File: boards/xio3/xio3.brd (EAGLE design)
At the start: 170 x 170 mm, 67 parts, among them J1 POWER_JACKPTH

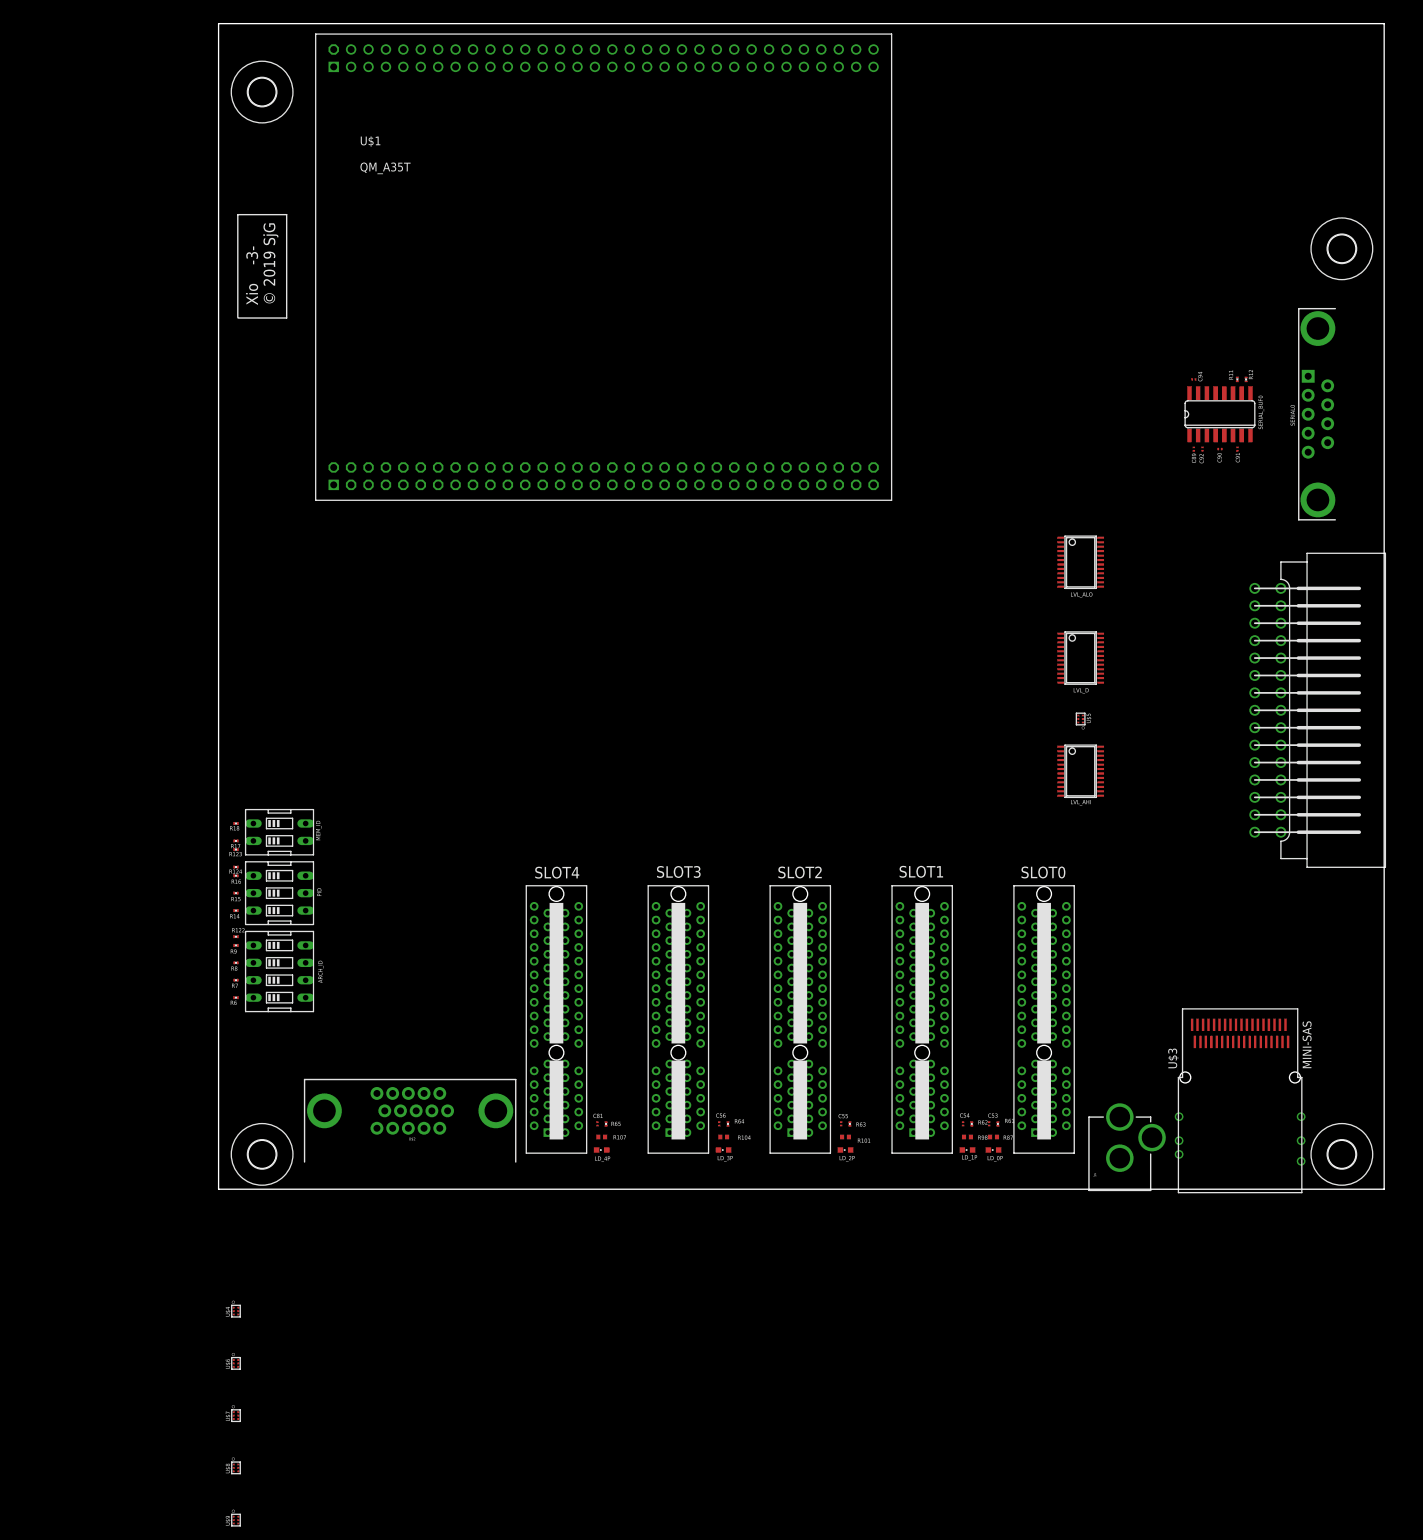
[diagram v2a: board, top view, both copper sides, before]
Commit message: Before deciding which signals to drop for S4,S5
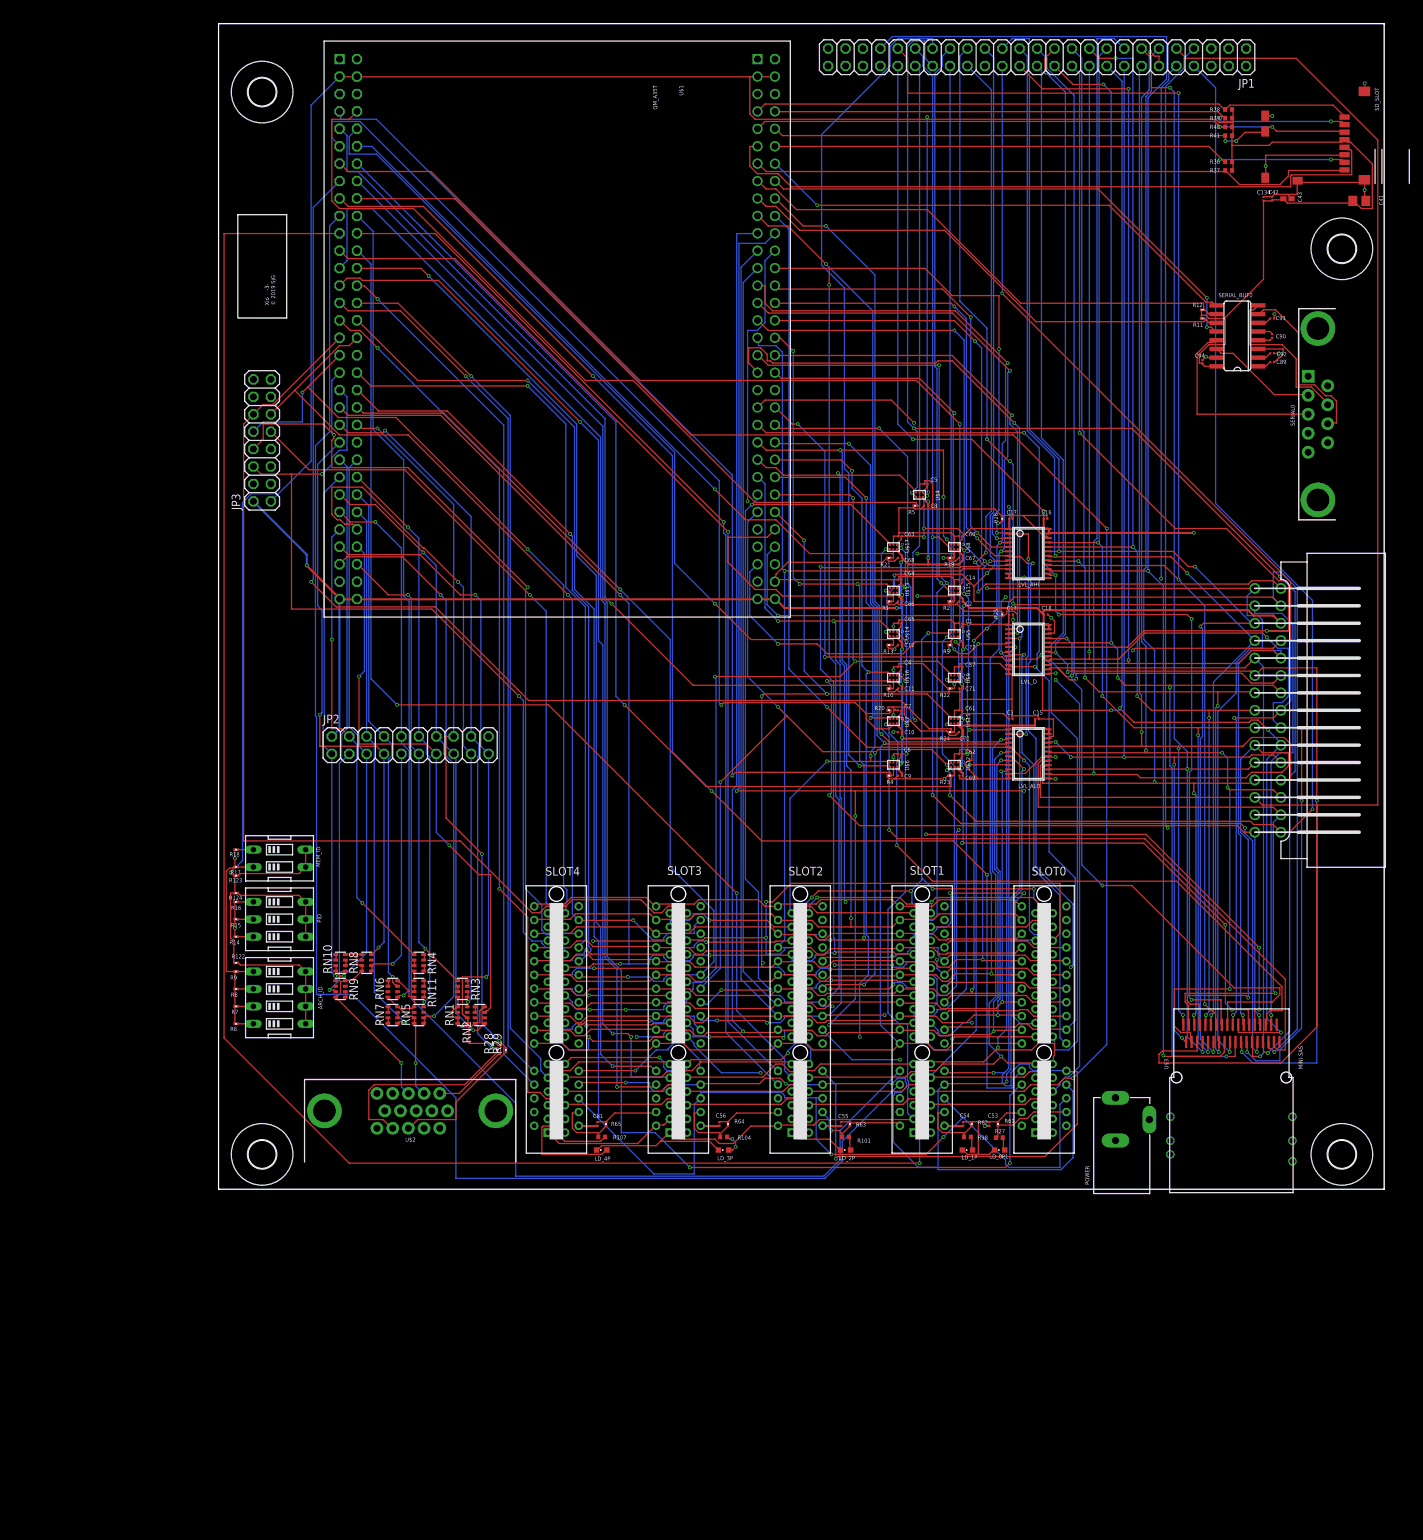
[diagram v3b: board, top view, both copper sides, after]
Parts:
- removed J1: POWER_JACKPTH, SparkFun:POWER_JACK_PTH
- removed LD_0P: SML-D12D1WT86, led:CHIPLED_0603
- removed R87: 59R, rcl:R0402
- added C1, C10, C11, C12, C13, C134, C14, C15, C16, C17, C18, C2, C3, C4, C5, C57, C6, C60, C61, C62, C63, C64, C65, C66, C67, C68, C69, C7, C70, C71, C72, C8, C9: 0.1uF, rcl:C0201
- added C41: 22uF, rcl:C0805
- added C42: 1uF, rcl:C0201
- added C43: 10uF, rcl:C0402K
- added JP1: (no value), pinhead:2X25
- added JP2: (no value), pinhead:2X10
- added JP3: (no value), pinhead:2X08
- added LD_0P1: SML-D12D1WT86, led:CHIPLED_0603
- added POWER: dc5vin, sjg-power:DCJ3P-14.2X11.0X9.0MM
- added R1, R10, R13, R19, R2, R20, R21, R22, R23, R24, R25, R26, R3, R4, R5: 10K, rcl:R0201
- added R27: 59R, rcl:R0402
- added R28, R29: 100R, rcl:R0201
- added R36, R37, R38, R39, R40, R41: 4K7, rcl:R0402
- added RN1, RN5, RN8: 1K, sjg-resistor:ACAS0612
- added RN10, RN11, RN2, RN3, RN4, RN6, RN7, RN9: 2K, sjg-resistor:ACAS0612
- added SD_SLOT: 5025700893, j_microsd_molex_5025700893:5025700893
- added U$11, U$12, U$13, U$14, U$15, U$16, U$17: 74LVC1T45GWSOT866, sjg-logic:SOT886
- moved U$8 170.3 mm to (107.3, 93.7), turned to 270 degrees
- moved U$9 161.5 mm to (107.3, 74.6), turned to 270 degrees
- moved U$4 155.3 mm to (102.2, 101.3), turned to 270 degrees
- moved U$7 139.5 mm to (98.4, 68.3), turned to 270 degrees
- moved U$6 129.7 mm to (98.4, 61.9), turned to 270 degrees
- moved LVL_AHI 32.7 mm to (118.1, 92.7)
- moved LVL_ALO 29.0 mm to (118.1, 63.5)
- moved U$5 22.2 mm to (107.3, 81.0), turned to 270 degrees
- moved C91 19.7 mm to (153.7, 127.0), turned to 0 degrees
- moved C90 18.2 mm to (153.7, 124.5), turned to 270 degrees
- moved C92 17.3 mm to (153.7, 121.9), turned to 0 degrees
- moved C89 17.1 mm to (153.7, 120.7), turned to 180 degrees
- moved R12 12.0 mm to (143.5, 128.3), turned to 0 degrees
- moved SERIAL_BUF0 11.7 mm to (148.6, 124.5), turned to 90 degrees
- moved U$1 11.3 mm to (49.4, 125.5), turned to 270 degrees
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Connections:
- removed net !H_CCTL!: CARTRIDGE.P15
- removed net !H_EXTSEL!: U$3.PB13
- removed net !H_HALT!: U$3.PA14
- removed net !H_IRQ!: U$3.PB14
- removed net !H_MPD!: U$3.PA15
- removed net !H_RST!: U$3.PA17
- removed net !H_S4!: CARTRIDGE.P1
- removed net !H_S5!: CARTRIDGE.P12
- removed net HOST_!EXTSEL!: SLOT0.B26, SLOT1.B26, SLOT2.B26, SLOT3.B26, SLOT4.B26
- removed net HOST_!HALT!: SLOT0.B27, SLOT1.B27, SLOT2.B27, SLOT3.B27, SLOT4.B27
- removed net HOST_!IRQ!: SLOT0.B28, SLOT1.B28, SLOT2.B28, SLOT3.B28, SLOT4.B28
- removed net HOST_!MPD!: SLOT0.B29, SLOT1.B29, SLOT2.B29, SLOT3.B29, SLOT4.B29
- removed net HOST_!REF!: SLOT0.B30, SLOT1.B30, SLOT2.B30, SLOT3.B30, SLOT4.B30
- removed net HOST_!RST!: SLOT0.B31, SLOT1.B31, SLOT2.B31, SLOT3.B31, SLOT4.B31
- removed net HOST_A0: SLOT0.A8, SLOT1.A8, SLOT2.A8, SLOT3.A8, SLOT4.A7
- removed net HOST_A1: SLOT0.A9, SLOT1.A9, SLOT2.A9, SLOT3.A9, SLOT4.A8
- removed net HOST_A10: SLOT0.A18, SLOT1.A18, SLOT2.A18, SLOT3.A18, SLOT4.A17
- removed net HOST_A11: SLOT0.A19, SLOT1.A19, SLOT2.A19, SLOT3.A19, SLOT4.A18
- removed net HOST_A12: SLOT0.A20, SLOT1.A20, SLOT2.A20, SLOT3.A20, SLOT4.A19
- removed net HOST_A13: SLOT0.A21, SLOT1.A21, SLOT2.A21, SLOT3.A21, SLOT4.A20
- removed net HOST_A14: SLOT0.A22, SLOT1.A22, SLOT2.A22, SLOT3.A22, SLOT4.A21
- removed net HOST_A15: SLOT0.A23, SLOT1.A23, SLOT2.A23, SLOT3.A23, SLOT4.A22
- removed net HOST_A2: SLOT0.A10, SLOT1.A10, SLOT2.A10, SLOT3.A10, SLOT4.A9
- removed net HOST_A3: SLOT0.A11, SLOT1.A11, SLOT2.A11, SLOT3.A11, SLOT4.A10
- removed net HOST_A4: SLOT0.A12, SLOT1.A12, SLOT2.A12, SLOT3.A12, SLOT4.A11
- removed net HOST_A5: SLOT0.A13, SLOT1.A13, SLOT2.A13, SLOT3.A13, SLOT4.A12
- removed net HOST_A6: SLOT0.A14, SLOT1.A14, SLOT2.A14, SLOT3.A14, SLOT4.A13
- removed net HOST_A7: SLOT0.A15, SLOT1.A15, SLOT2.A15, SLOT3.A15, SLOT4.A14
- removed net HOST_A8: SLOT0.A16, SLOT1.A16, SLOT2.A16, SLOT3.A16, SLOT4.A15
- removed net HOST_A9: SLOT0.A17, SLOT1.A17, SLOT2.A17, SLOT3.A17, SLOT4.A16
- removed net HOST_CLK: SLOT0.A24, SLOT1.A24, SLOT2.A24, SLOT3.A24, SLOT4.A23
- removed net HOST_D0: SLOT0.A25, SLOT1.A25, SLOT2.A25, SLOT3.A25, SLOT4.A24
- removed net HOST_D1: SLOT0.A26, SLOT1.A26, SLOT2.A26, SLOT3.A26, SLOT4.A25
- removed net HOST_D2: SLOT0.A27, SLOT1.A27, SLOT2.A27, SLOT3.A27, SLOT4.A26
- removed net HOST_D3: SLOT0.A28, SLOT1.A28, SLOT2.A28, SLOT3.A28, SLOT4.A27
- removed net HOST_D4: SLOT0.A29, SLOT1.A29, SLOT2.A29, SLOT3.A29, SLOT4.A28
- removed net HOST_D5: SLOT0.A30, SLOT1.A30, SLOT2.A30, SLOT3.A30, SLOT4.A29
- removed net HOST_D6: SLOT0.A31, SLOT1.A31, SLOT2.A31, SLOT3.A31, SLOT4.A30
- removed net HOST_D7: SLOT0.A32, SLOT1.A32, SLOT2.A32, SLOT3.A32, SLOT4.A31
- removed net HOST_R/!W!: SLOT0.B32, SLOT1.B32, SLOT2.B32, SLOT3.B32, SLOT4.B32
- removed net H_A0: CARTRIDGE.P5, LVL_ALO.21, U$3.PA1
- removed net H_A1: CARTRIDGE.P4, LVL_ALO.20, U$3.PB1
- removed net H_A10: CARTRIDGE.PP, LVL_AHI.19, U$3.PA6
- removed net H_A11: CARTRIDGE.PN, LVL_AHI.18, U$3.PB6
- removed net H_A12: CARTRIDGE.PK, LVL_AHI.17, U$3.PA7
- removed net H_A13: LVL_AHI.16, U$3.PB7
- removed net H_A14: LVL_AHI.15, U$3.PA8
- removed net H_A15: LVL_AHI.14, U$3.PB8
- removed net H_A2: CARTRIDGE.P3, LVL_ALO.19, U$3.PA2
- removed net H_A3: CARTRIDGE.P2, LVL_ALO.18, U$3.PB2
- removed net H_A4: CARTRIDGE.PC, LVL_ALO.17, U$3.PA3
- removed net H_A5: CARTRIDGE.PD, LVL_ALO.16, U$3.PB3
- removed net H_A6: CARTRIDGE.PE, LVL_ALO.15, U$3.PA4
- removed net H_A7: CARTRIDGE.PF, LVL_ALO.14, U$3.PB4
- removed net H_A8: CARTRIDGE.PH, LVL_AHI.21, U$3.PA5
- removed net H_A9: CARTRIDGE.PJ, LVL_AHI.20, U$3.PB5
- removed net H_CLK: CARTRIDGE.PS, U$3.PA9
- removed net H_D0: CARTRIDGE.P10, LVL_D.21, U$3.PB9
- removed net H_D1: CARTRIDGE.P9, LVL_D.20, U$3.PA10
- removed net H_D2: CARTRIDGE.P8, LVL_D.19, U$3.PB10
- removed net H_D3: CARTRIDGE.PL, LVL_D.18, U$3.PA11
- removed net H_D4: CARTRIDGE.P6, LVL_D.17, U$3.PB11
- removed net H_D5: CARTRIDGE.P7, LVL_D.16, U$3.PA12
- removed net H_D6: CARTRIDGE.P11, LVL_D.15, U$3.PB12
- removed net H_D7: CARTRIDGE.PM, LVL_D.14, U$3.PA13
- removed net H_R/!W!: CARTRIDGE.PR, U$3.PB17
- removed net H_RD4: CARTRIDGE.PA, U$3.PB15
- removed net H_RD5: CARTRIDGE.P14, U$3.PA16
- removed net H_REF: U$3.PB16
- removed net N$82: LD_0P.A, R87.2
- removed net SBUS12_CTL0: SLOT0.B8, SLOT1.B8
- removed net SBUS12_CTL1: SLOT0.B9, SLOT1.B9
- removed net SBUS12_CTL2: SLOT0.B10, SLOT1.B10
- removed net SBUS12_CTL3: SLOT0.B11, SLOT1.B11
- removed net SBUS12_CTL4: SLOT0.B12, SLOT1.B12
- removed net SBUS12_D0: SLOT0.B18, SLOT1.B18
- removed net SBUS12_D1: SLOT0.B19, SLOT1.B19
- removed net SBUS12_D2: SLOT0.B20, SLOT1.B20
- removed net SBUS12_D3: SLOT0.B21, SLOT1.B21
- removed net SBUS12_D4: SLOT0.B22, SLOT1.B22
- removed net SBUS12_D5: SLOT0.B23, SLOT1.B23
- removed net SBUS12_D6: SLOT0.B24, SLOT1.B24
- removed net SBUS12_D7: SLOT0.B25, SLOT1.B25
- removed net SBUS34_CTL0: SLOT2.B8, SLOT3.B8
- removed net SBUS34_CTL1: SLOT2.B9, SLOT3.B9
- removed net SBUS34_CTL2: SLOT2.B10, SLOT3.B10
- removed net SBUS34_CTL3: SLOT2.B11, SLOT3.B11
- removed net SBUS34_CTL4: SLOT2.B12, SLOT3.B12
- removed net SBUS34_D0: SLOT2.B18, SLOT3.B18
- removed net SBUS34_D1: SLOT2.B19, SLOT3.B19
- removed net SBUS34_D2: SLOT2.B20, SLOT3.B20
- removed net SBUS34_D3: SLOT2.B21, SLOT3.B21
- removed net SBUS34_D4: SLOT2.B22, SLOT3.B22
- removed net SBUS34_D5: SLOT2.B23, SLOT3.B23
- removed net SBUS34_D6: SLOT2.B24, SLOT3.B24
- removed net SBUS34_D7: SLOT2.B25, SLOT3.B25
- removed net SPI_CLK: SLOT0.B17, SLOT1.B17, SLOT2.B17, SLOT3.B17, SLOT4.B17
- removed net SPI_IRQ0: SLOT0.B14
- removed net SPI_IRQ1: SLOT1.B14
- removed net SPI_IRQ2: SLOT2.B14
- removed net SPI_IRQ3: SLOT3.B14
- removed net SPI_IRQ4: SLOT4.B14
- removed net SPI_MISO: SLOT0.B16, SLOT1.B16, SLOT2.B16, SLOT3.B16, SLOT4.B16
- removed net SPI_MOSI: SLOT0.B15, SLOT1.B15, SLOT2.B15, SLOT3.B15, SLOT4.B15
- removed net SPI_SS0: SLOT0.B13
- removed net SPI_SS1: SLOT1.B13
- removed net SPI_SS2: SLOT2.B13
- removed net SPI_SS3: SLOT3.B13
- removed net SPI_SS4: SLOT4.B13
- new net !HI_CCTL!: CARTRIDGE.P15, JP1.34, U$13.4, U$3.PA18
- new net !HI_EXTSEL!: JP1.36, U$3.PB13, U$5.4
- new net !HI_HALT!: JP1.39, U$3.PA14, U$8.4
- new net !HI_IRQ!: JP1.37, U$3.PB14, U$6.4
- new net !HI_MPD!: JP1.38, U$3.PA15, U$4.4
- new net !HI_REF!: JP1.40, U$3.PB16, U$7.4
- new net !HI_RST!: JP1.32, U$17.4, U$3.PA17
- new net !HI_S4!: CARTRIDGE.P1, JP1.8, U$12.4
- new net !HI_S5!: CARTRIDGE.P12, JP1.30, U$11.4
- new net !LO_CCTL!: SLOT0.A27, SLOT1.A27, SLOT2.A27, SLOT3.A27, SLOT4.A27, U$1.U7_34, U$13.3
- new net !LO_EXTSEL!: SLOT0.A29, SLOT1.A29, SLOT2.A29, SLOT3.A29, SLOT4.A29, U$1.U7_44, U$5.3
- new net !LO_HALT!: SLOT0.A30, SLOT1.A30, SLOT2.A30, SLOT3.A30, SLOT4.A30, U$1.U7_45, U$8.3
- new net !LO_IRQ!: SLOT0.A31, SLOT1.A31, SLOT2.A31, SLOT3.A31, SLOT4.A31, U$1.U7_46, U$6.3
- new net !LO_MPD!: SLOT0.A32, SLOT1.A32, SLOT2.A32, SLOT3.A32, SLOT4.A32, U$1.U7_47, U$4.3
- new net !LO_REF!: SLOT0.B17, SLOT1.B17, SLOT2.B17, SLOT3.B17, SLOT4.B17, U$1.U7_50, U$7.3
- new net !LO_RST!: SLOT0.B18, SLOT1.B18, SLOT2.B18, SLOT3.B18, SLOT4.B18, U$1.U7_51, U$17.3
- new net !LO_S4!: SLOT0.B20, SLOT1.B20, SLOT2.B20, SLOT3.B20, SLOT4.B20, U$1.U7_53, U$12.3
- new net !LO_S5!: SLOT0.B21, SLOT1.B21, SLOT2.B21, SLOT3.B21, SLOT4.B21, U$1.U7_54, U$11.3
- new net DIR_A: LVL_AHI.2, LVL_ALO.2, R26.1, U$1.U7_55
- new net DIR_CCTL: R1.1, U$1.U7_56, U$13.5
- new net DIR_CLK: R2.1, U$1.U7_57, U$15.5
- new net DIR_D: LVL_D.2, R25.1, U$1.U7_58
- new net DIR_EXTSEL: R3.1, U$1.U7_59, U$5.5
- new net DIR_HALT: R19.1, U$1.U7_60, U$8.5
- new net DIR_IRQ: R4.1, U$1.U8_7, U$6.5
- new net DIR_MPD: R5.1, U$1.U8_8, U$4.5
- new net DIR_RD4: R10.1, U$1.U8_9, U$16.5
- new net DIR_RD5: R13.1, U$1.U8_10, U$14.5
- new net DIR_REF: R20.1, U$1.U8_11, U$7.5
- new net DIR_RST: R21.1, U$1.U8_12, U$17.5
- new net DIR_RW: R22.1, U$1.U8_13, U$9.5
- new net DIR_S4: R23.1, U$1.U8_14, U$12.5
- new net DIR_S5: R24.1, U$1.U8_15, U$11.5
- new net HBUS0: JP3.3, SLOT0.B22, SLOT1.B22, SLOT2.B22, SLOT3.B22, SLOT4.B22, U$1.U8_42
- new net HBUS1: JP3.4, SLOT0.B23, SLOT1.B23, SLOT2.B23, SLOT3.B23, SLOT4.B23, U$1.U8_41
- new net HBUS2: JP3.5, SLOT0.B24, SLOT1.B24, SLOT2.B24, SLOT3.B24, SLOT4.B24, U$1.U8_40
- new net HBUS3: JP3.6, SLOT0.B25, SLOT1.B25, SLOT2.B25, SLOT3.B25, SLOT4.B25, U$1.U8_39
- new net HBUS4: JP3.7, SLOT0.B26, SLOT1.B26, SLOT2.B26, SLOT3.B26, SLOT4.B26, U$1.U8_38
- new net HBUS5: JP3.8, SLOT0.B27, SLOT1.B27, SLOT2.B27, SLOT3.B27, SLOT4.B27, U$1.U8_37
- new net HBUS6: JP3.9, SLOT0.B28, SLOT1.B28, SLOT2.B28, SLOT3.B28, SLOT4.B28, U$1.U8_36
- new net HBUS7: JP3.10, SLOT0.B29, SLOT1.B29, SLOT2.B29, SLOT3.B29, SLOT4.B29, U$1.U8_35
- new net HBUS8: JP3.11, SLOT0.B30, SLOT1.B30, SLOT2.B30, SLOT3.B30, SLOT4.B30, U$1.U8_34
- new net HBUS9: JP3.12, SLOT0.B31, SLOT1.B31, SLOT2.B31, SLOT3.B31, SLOT4.B31, U$1.U8_33
- new net HI_A0: CARTRIDGE.P5, JP1.16, LVL_ALO.21, U$3.PA1
- new net HI_A1: CARTRIDGE.P4, JP1.14, LVL_ALO.20, U$3.PB1
- new net HI_A10: CARTRIDGE.PP, JP1.29, LVL_AHI.19, U$3.PA6
- new net HI_A11: CARTRIDGE.PN, JP1.27, LVL_AHI.18, U$3.PB6
- new net HI_A12: CARTRIDGE.PK, JP1.21, LVL_AHI.17, U$3.PA7
- new net HI_A13: JP1.41, LVL_AHI.16, U$3.PB7
- new net HI_A14: JP1.43, LVL_AHI.15, U$3.PA8
- new net HI_A15: JP1.42, LVL_AHI.14, U$3.PB8
- new net HI_A2: CARTRIDGE.P3, JP1.12, LVL_ALO.19, U$3.PA2
- new net HI_A3: CARTRIDGE.P2, JP1.10, LVL_ALO.18, U$3.PB2
- new net HI_A4: CARTRIDGE.PC, JP1.9, LVL_ALO.17, U$3.PA3
- new net HI_A5: CARTRIDGE.PD, JP1.11, LVL_ALO.16, U$3.PB3
- new net HI_A6: CARTRIDGE.PE, JP1.13, LVL_ALO.15, U$3.PA4
- new net HI_A7: CARTRIDGE.PF, JP1.15, LVL_ALO.14, U$3.PB4
- new net HI_A8: CARTRIDGE.PH, JP1.17, LVL_AHI.21, U$3.PA5
- new net HI_A9: CARTRIDGE.PJ, JP1.19, LVL_AHI.20, U$3.PB5
- new net HI_CLK: CARTRIDGE.PS, JP1.35, U$15.4, U$3.PA9
- new net HI_D0: CARTRIDGE.P10, JP1.26, LVL_D.21, U$3.PB9
- new net HI_D1: CARTRIDGE.P9, JP1.24, LVL_D.20, U$3.PA10
- new net HI_D2: CARTRIDGE.P8, JP1.22, LVL_D.19, U$3.PB10
- new net HI_D3: CARTRIDGE.PL, JP1.23, LVL_D.18, U$3.PA11
- new net HI_D4: CARTRIDGE.P6, JP1.18, LVL_D.17, U$3.PB11
- new net HI_D5: CARTRIDGE.P7, JP1.20, LVL_D.16, U$3.PA12
- new net HI_D6: CARTRIDGE.P11, JP1.28, LVL_D.15, U$3.PB12
- new net HI_D7: CARTRIDGE.PM, JP1.25, LVL_D.14, U$3.PA13
- new net HI_R/!W!: CARTRIDGE.PR, JP1.33, U$3.PB17, U$9.4
- new net HI_RD4: CARTRIDGE.PA, JP1.7, U$16.4, U$3.PB15
- new net HI_RD5: CARTRIDGE.P14, JP1.31, U$14.4, U$3.PA16
- new net LO_A0: LVL_ALO.3, SLOT0.A11, SLOT1.A11, SLOT2.A11, SLOT3.A11, SLOT4.A11, U$1.U7_18
- new net LO_A1: LVL_ALO.4, SLOT0.A12, SLOT1.A12, SLOT2.A12, SLOT3.A12, SLOT4.A12, U$1.U7_19
- new net LO_A10: LVL_AHI.5, SLOT0.A21, SLOT1.A21, SLOT2.A21, SLOT3.A21, SLOT4.A21, U$1.U7_28
- new net LO_A11: LVL_AHI.6, SLOT0.A22, SLOT1.A22, SLOT2.A22, SLOT3.A22, SLOT4.A22, U$1.U7_29
- new net LO_A12: LVL_AHI.7, SLOT0.A23, SLOT1.A23, SLOT2.A23, SLOT3.A23, SLOT4.A23, U$1.U7_30
- new net LO_A13: LVL_AHI.8, SLOT0.A24, SLOT1.A24, SLOT2.A24, SLOT3.A24, SLOT4.A24, U$1.U7_31
- new net LO_A14: LVL_AHI.9, SLOT0.A25, SLOT1.A25, SLOT2.A25, SLOT3.A25, SLOT4.A25, U$1.U7_32
- new net LO_A15: LVL_AHI.10, SLOT0.A26, SLOT1.A26, SLOT2.A26, SLOT3.A26, SLOT4.A26, U$1.U7_33
- new net LO_A2: LVL_ALO.5, SLOT0.A13, SLOT1.A13, SLOT2.A13, SLOT3.A13, SLOT4.A13, U$1.U7_20
- new net LO_A3: LVL_ALO.6, SLOT0.A14, SLOT1.A14, SLOT2.A14, SLOT3.A14, SLOT4.A14, U$1.U7_21
- new net LO_A4: LVL_ALO.7, SLOT0.A15, SLOT1.A15, SLOT2.A15, SLOT3.A15, SLOT4.A15, U$1.U7_22
- new net LO_A5: LVL_ALO.8, SLOT0.A16, SLOT1.A16, SLOT2.A16, SLOT3.A16, SLOT4.A16, U$1.U7_23
- new net LO_A6: LVL_ALO.9, SLOT0.A17, SLOT1.A17, SLOT2.A17, SLOT3.A17, SLOT4.A17, U$1.U7_24
- new net LO_A7: LVL_ALO.10, SLOT0.A18, SLOT1.A18, SLOT2.A18, SLOT3.A18, SLOT4.A18, U$1.U7_25
- new net LO_A8: LVL_AHI.3, SLOT0.A19, SLOT1.A19, SLOT2.A19, SLOT3.A19, SLOT4.A19, U$1.U7_26
- new net LO_A9: LVL_AHI.4, SLOT0.A20, SLOT1.A20, SLOT2.A20, SLOT3.A20, SLOT4.A20, U$1.U7_27
- new net LO_CLK: SLOT0.A28, SLOT1.A28, SLOT2.A28, SLOT3.A28, SLOT4.A28, U$1.U7_35, U$15.3
- new net LO_D0: LVL_D.3, SLOT0.B7, SLOT1.B7, SLOT2.B7, SLOT3.B7, SLOT4.B7, U$1.U7_36
- new net LO_D1: LVL_D.4, SLOT0.B8, SLOT1.B8, SLOT2.B8, SLOT3.B8, SLOT4.B8, U$1.U7_37
- new net LO_D2: LVL_D.5, SLOT0.B9, SLOT1.B9, SLOT2.B9, SLOT3.B9, SLOT4.B9, U$1.U7_38
- new net LO_D3: LVL_D.6, SLOT0.B10, SLOT1.B10, SLOT2.B10, SLOT3.B10, SLOT4.B10, U$1.U7_39
- new net LO_D4: LVL_D.7, SLOT0.B11, SLOT1.B11, SLOT2.B11, SLOT3.B11, SLOT4.B11, U$1.U7_40
- new net LO_D5: LVL_D.8, SLOT0.B12, SLOT1.B12, SLOT2.B12, SLOT3.B12, SLOT4.B12, U$1.U7_41
- new net LO_D6: LVL_D.9, SLOT0.B13, SLOT1.B13, SLOT2.B13, SLOT3.B13, SLOT4.B13, U$1.U7_42
- new net LO_D7: LVL_D.10, SLOT0.B14, SLOT1.B14, SLOT2.B14, SLOT3.B14, SLOT4.B14, U$1.U7_43
- new net LO_R/!W!: SLOT0.B19, SLOT1.B19, SLOT2.B19, SLOT3.B19, SLOT4.B19, U$1.U7_52, U$9.3
- new net LO_RD4: SLOT0.B15, SLOT1.B15, SLOT2.B15, SLOT3.B15, SLOT4.B15, U$1.U7_48, U$16.3
- new net LO_RD5: SLOT0.B16, SLOT1.B16, SLOT2.B16, SLOT3.B16, SLOT4.B16, U$1.U7_49, U$14.3
- new net N$1: LD_0P1.A, R27.2
- new net N$10: RN7.3B, RN7.4B
- new net N$12: RN4.1B, RN4.2B
- new net N$13: RN4.3B, RN4.4B
- new net N$14: RN11.1A, RN4.4A
- new net N$15: RN11.1B, RN11.2B
- new net N$16: RN11.2A, RN11.3A
- new net N$17: RN11.3B, RN11.4B
- new net N$19: RN9.3B, RN9.4B
- new net N$2: RN4.2A, RN4.3A
- new net N$20: RN10.1B, RN10.2B
- new net N$21: RN10.2A, RN10.3A
- new net N$22: RN10.3B, RN10.4B
- new net N$3: RN2.3B, RN2.4B
- new net N$4: RN3.1B, RN3.2B
- new net N$5: RN3.2A, RN3.3A
- new net N$6: RN3.3B, RN3.4B
- new net N$7: RN6.3B, RN6.4B
- new net N$8: RN7.1B, RN7.2B
- new net N$9: RN7.2A, RN7.3A
- new net SD0: R36.1, SD_SLOT.P$7, U$1.U7_12
- new net SD1: R37.1, SD_SLOT.P$8, U$1.U7_13
- new net SD2: R38.1, SD_SLOT.P$1, U$1.U7_7
- new net SD3: R39.1, SD_SLOT.P$2, U$1.U7_8
- new net SDCD: R41.1, SD_SLOT.DTCT, U$1.U7_10
- new net SDCLK: SD_SLOT.P$5, U$1.U7_11
- new net SDCMD: R40.1, SD_SLOT.P$3, U$1.U7_9
- new net SPI0_IRQ: SLOT0.A8, U$1.U8_16
- new net SPI0_MOSI: SLOT0.A9, U$1.U8_18
- new net SPI1_IRQ: SLOT1.A8, U$1.U8_19
- new net SPI1_MISO: SLOT1.A10, U$1.U8_20
- new net SPI1_MOSI: SLOT1.A9, U$1.U8_21
- new net SPI2_IRQ: SLOT2.A8, U$1.U8_22
- new net SPI2_MISO: SLOT2.A10, U$1.U8_23
- new net SPI2_MOSI: SLOT2.A9, U$1.U8_24
- new net SPI3_IRQ: SLOT3.A8, U$1.U8_25
- new net SPI3_MISO: SLOT3.A10, U$1.U8_26
- new net SPI3_MOSI: SLOT3.A9, U$1.U8_27
- new net SPI4_IRQ: SLOT4.A8, U$1.U8_28
- new net SPI4_MISO: SLOT4.A10, U$1.U8_29
- new net SPI4_MOSI: SLOT4.A9, U$1.U8_30
- new net SPIO_MISO: SLOT0.A10, U$1.U8_17
- new net VALID_RD: SLOT0.B5, SLOT1.B5, SLOT2.B5, SLOT3.B5, SLOT4.B5, U$1.U8_31
- new net VALID_WR: SLOT0.B6, SLOT1.B6, SLOT2.B6, SLOT3.B6, SLOT4.B6, U$1.U8_32
- new net VGA_B0: JP2.1, RN10.1A, U$1.U8_49
- new net VGA_B1: JP2.3, RN9.3A, U$1.U8_47
- new net VGA_B2: JP2.5, RN9.1A, U$1.U8_48
- new net VGA_B3: JP2.7, RN8.4A, U$1.U8_45
- new net VGA_B4: JP2.9, RN8.1A, RN8.2A, U$1.U8_46
- new net VGA_BLU: RN10.4A, RN8.1B, RN8.2B, RN8.4B, RN9.1B, RN9.4A, U$2.3
- new net VGA_G0: JP2.4, RN4.1A, U$1.U8_55
- new net VGA_G1: JP2.6, RN7.1A, U$1.U8_54
- new net VGA_G2: JP2.8, RN6.3A, U$1.U8_52
- new net VGA_G3: JP2.10, RN6.1A, U$1.U8_53
- new net VGA_G4: JP2.12, RN5.4A, U$1.U8_50
- new net VGA_G5: JP2.14, RN5.1A, RN5.2A, U$1.U8_51
- new net VGA_GRN: RN11.4A, RN5.1B, RN5.2B, RN5.4B, RN6.1B, RN6.4A, RN7.4A, U$2.2
- new net VGA_HS: R29.1, U$2.13
- new net VGA_HSYNC: JP2.16, R29.2, U$1.U8_44
- new net VGA_R0: JP2.11, RN3.1A, U$1.U8_60
- new net VGA_R1: JP2.13, RN2.3A, U$1.U8_58
- new net VGA_R2: JP2.15, RN2.1A, U$1.U8_59
- new net VGA_R3: JP2.17, RN1.4A, U$1.U8_56
- new net VGA_R4: JP2.19, RN1.1A, RN1.2A, U$1.U8_57
- new net VGA_RED: RN1.1B, RN1.2B, RN1.4B, RN2.1B, RN2.4A, RN3.4A, U$2.1
- new net VGA_VS: R28.1, U$2.14
- new net VGA_VSYNC: JP2.18, R28.2, U$1.U8_43
- net +3V3: now also C1.1, C13.1, C134.2, C14.1, C17.1, C3.1, C4.1, C41.1, C42.1, C43.1, C5.1, C57.1, C6.1, C60.1, C61.1, C62.1, C63.1, C64.1, C65.1, C7.1, JP3.1, R36.2, R37.2, R38.2, R39.2, R40.2, R41.2, SD_SLOT.P$4, U$1.U7_3, U$1.U7_4, U$1.U8_3, U$1.U8_4, U$11.1, U$12.1, U$13.1, U$14.1, U$15.1, U$16.1, U$17.1; no longer LVL_AHI.2, LVL_ALO.2, SLOT0.B5, SLOT0.B6, SLOT0.B7, SLOT1.B5, SLOT1.B6, SLOT1.B7, SLOT2.B5, SLOT2.B6, SLOT2.B7, SLOT3.B5, SLOT3.B6, SLOT3.B7, SLOT4.B5, SLOT4.B6, SLOT4.B7, U$4.5, U$5.5, U$6.5, U$7.5, U$8.5, U$9.5
- net +5V: now also C10.1, C11.1, C12.1, C15.1, C16.1, C18.1, C2.1, C66.1, C67.1, C68.1, C69.1, C70.1, C71.1, C72.1, C8.1, C9.1, JP1.1, JP1.2, JP1.3, JP1.4, JP1.5, JP1.6, JP2.2, JP3.2, POWER.+, U$1.U7_63, U$1.U7_64, U$1.U8_63, U$1.U8_64, U$11.6, U$12.6, U$13.6, U$14.6, U$15.6, U$16.6, U$17.6
- net GND: now also C1.2, C10.2, C11.2, C12.2, C13.2, C134.1, C14.2, C15.2, C16.2, C17.2, C18.2, C2.2, C3.2, C4.2, C41.2, C42.2, C43.2, C5.2, C57.2, C6.2, C60.2, C61.2, C62.2, C63.2, C64.2, C65.2, C66.2, C67.2, C68.2, C69.2, C7.2, C70.2, C71.2, C72.2, C8.2, C9.2, JP1.44, JP1.45, JP1.46, JP1.47, JP1.48, JP1.49, JP1.50, JP2.20, JP3.13, JP3.14, JP3.15, JP3.16, LD_0P1.C, POWER.-1, R1.2, R10.2, R13.2, R19.2, R2.2, R20.2, R21.2, R22.2, R23.2, R24.2, R25.2, R26.2, R3.2, R4.2, R5.2, SD_SLOT.GND0, SD_SLOT.GND1, SD_SLOT.GND2, SD_SLOT.GND3, SD_SLOT.GND4, SD_SLOT.P$6, U$1.U7_1, U$1.U7_2, U$1.U7_5, U$1.U7_6, U$1.U7_61, U$1.U7_62, U$1.U8_1, U$1.U8_2, U$1.U8_5, U$1.U8_6, U$1.U8_61, U$1.U8_62, U$11.2, U$12.2, U$13.2, U$14.2, U$15.2, U$16.2, U$17.2, U$2.10, U$2.5, U$2.6, U$2.7, U$2.8; no longer LD_0P.C, SLOT4.B10, SLOT4.B11, SLOT4.B12, SLOT4.B18, SLOT4.B19, SLOT4.B20, SLOT4.B21, SLOT4.B22, SLOT4.B23, SLOT4.B24, SLOT4.B25, SLOT4.B8, SLOT4.B9
- net MCU_CTS: now also U$1.U7_14
- net MCU_RTS: now also U$1.U7_15
- net MCU_RX: now also U$1.U7_16
- net MCU_TX: now also U$1.U7_17
- net S0_PRESENT: now also R27.1; no longer R87.1
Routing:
- net +3V3: track 0.00 -> 687.3 mm, vias 0 -> 18
- net GND: track 0.00 -> 439.8 mm, vias 0 -> 24
- net +5V: track 0.00 -> 337.0 mm, vias 0 -> 17
- net LO_D1: track 0.00 -> 270.5 mm, vias 0 -> 6
- net LO_A4: track 0.00 -> 264.7 mm, vias 0 -> 6
- net SPI1_MOSI: track 0.00 -> 256.0 mm, vias 0 -> 1
- net LO_D3: track 0.00 -> 255.2 mm, vias 0 -> 5
- net VALID_WR: track 0.00 -> 255.0 mm, vias 0 -> 3
- net LO_A8: track 0.00 -> 254.0 mm, vias 0 -> 5
- net HI_A4: track 0.00 -> 253.6 mm
- net HBUS5: track 0.00 -> 237.8 mm, vias 0 -> 4
- net LO_A3: track 0.00 -> 237.4 mm, vias 0 -> 3
- net HI_RD4: track 0.00 -> 235.0 mm, vias 0 -> 4
- net HI_RD5: track 0.00 -> 231.4 mm, vias 0 -> 4
- net !LO_S4!: track 0.00 -> 230.6 mm, vias 0 -> 5
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- added copper zone on layer 2, net +5V
- added copper zone on layer 15, net GND
